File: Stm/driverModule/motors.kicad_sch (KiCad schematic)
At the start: 4 parts, among them U201 DRV8838, U202 DRV8838, U203 DRV8838, U204 VNH5019A-E

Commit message: Add Headers
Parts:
- added C201: 33nF, symbol Device:C
- added J201: Conn_02x05_Row_Letter_First, Connector_PinHeader_1.00mm:PinHeader_1x40_P1.00mm_Vertical, symbol Connector_Generic:Conn_02x05_Row_Letter_First
- added R201, R202, R205, R206: 1K, symbol Device:R_US
- added R203: 1K5, symbol Device:R_US
- added R204: 10K, symbol Device:R_US
- added R207, R208: 3K3, symbol Device:R_US
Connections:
- net +12V: now also U204.12 (VBAT)
- net +3V3: now also R201.1, R202.1, R207.1, R208.1
- net GND: now also C201.2, R203.2
- net MirrorMorotYA: now reaches U202.2 (OUT1)
- net MirrorMorotYA: now also J201.a2 (Pin_a2)
- net MirrorMotorYB: now reaches U202.3 (OUT2)
- net MirrorMotorYB: now also J201.a3 (Pin_a3)
- net MirrorMotorYEnable: now reaches U202.5 (EN)
- net MirrorYDirection: now reaches U202.6 (PH)
- net MirrorMotorXA: now reaches U203.2 (OUT1)
- net MirrorMotorXA: now also J201.b2 (Pin_b2)
- net MirrorMotorXB: now reaches U203.3 (OUT2)
- net MirrorMotorXB: now also J201.a4 (Pin_a4)
- net MirrorMotorXEnable: now reaches U203.5 (EN)
- net MirrorXDirection: now reaches U203.6 (PH)
- net at U204.10 (INB): now also R206.2, R208.2
- net at U204.4 (INA): now also R205.2, R207.2
- net at U204.5 (EN/DIAGA): now also R201.2
- net at U204.8 (CS): now also R203.1, R204.2
- net at U204.9 (EN/DIAGB): now also R202.2
- new net: C201.1, R204.1
- new net WindorMotorDirA: R205.1
- new net WindowMotorDirB: R206.1
- no-connect marks 0 -> 6
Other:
- moved on the sheet: U204

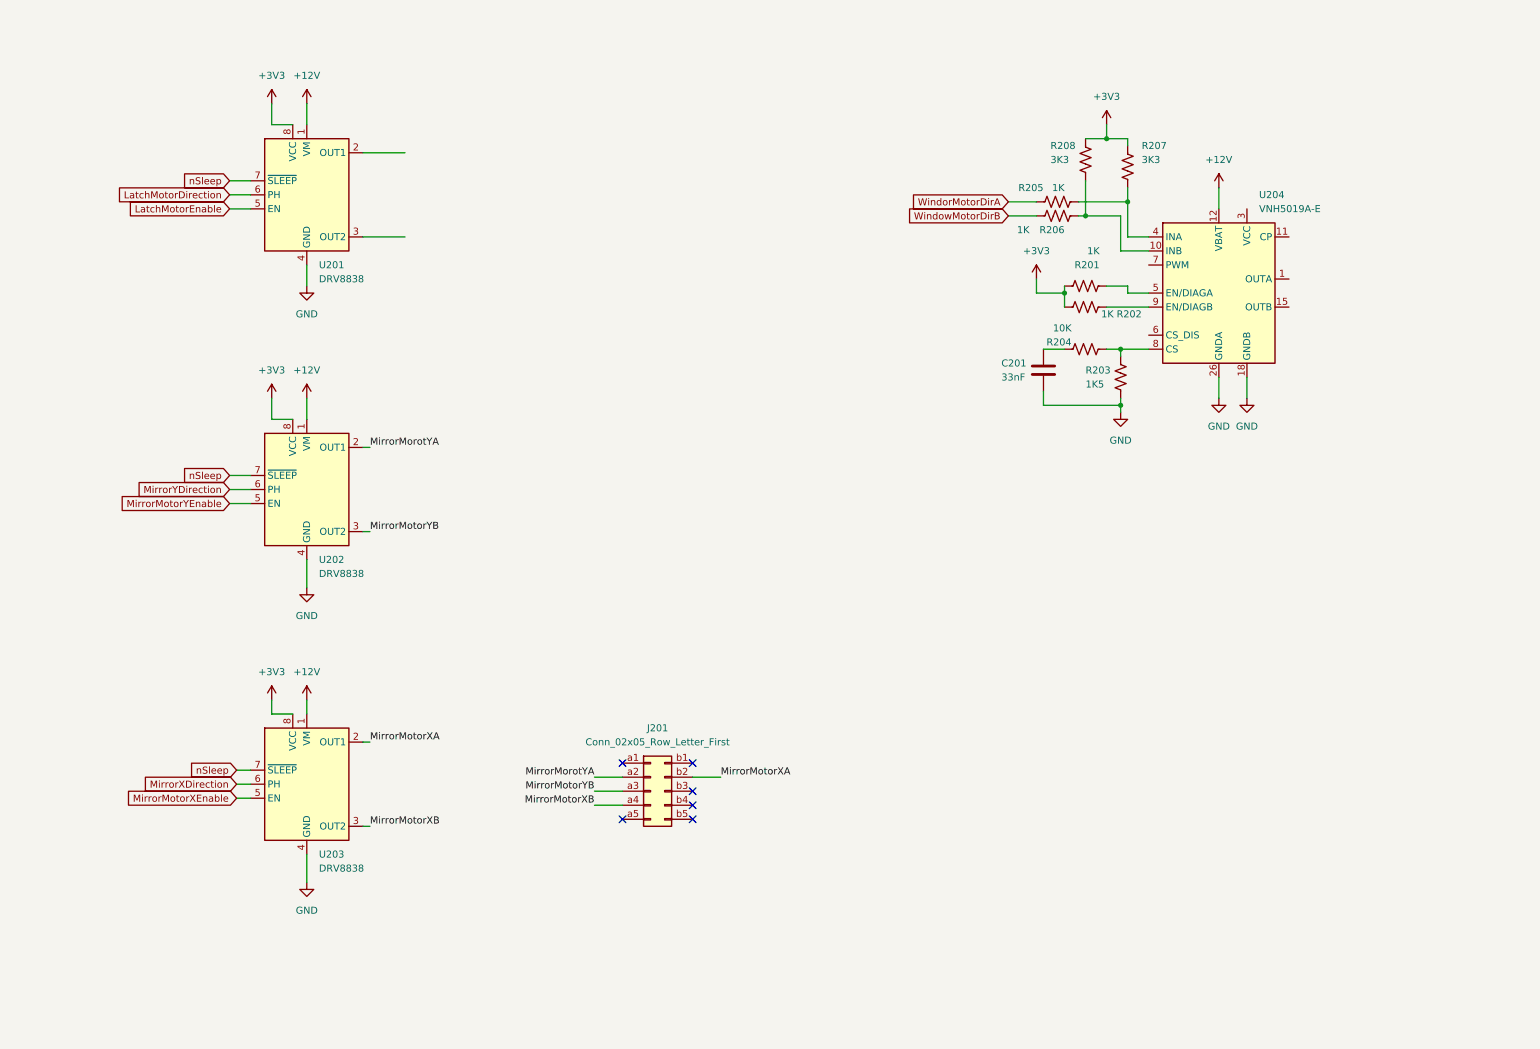
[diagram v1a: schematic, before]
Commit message: CD40109BNSR
Added low to high level shifter
and foot print
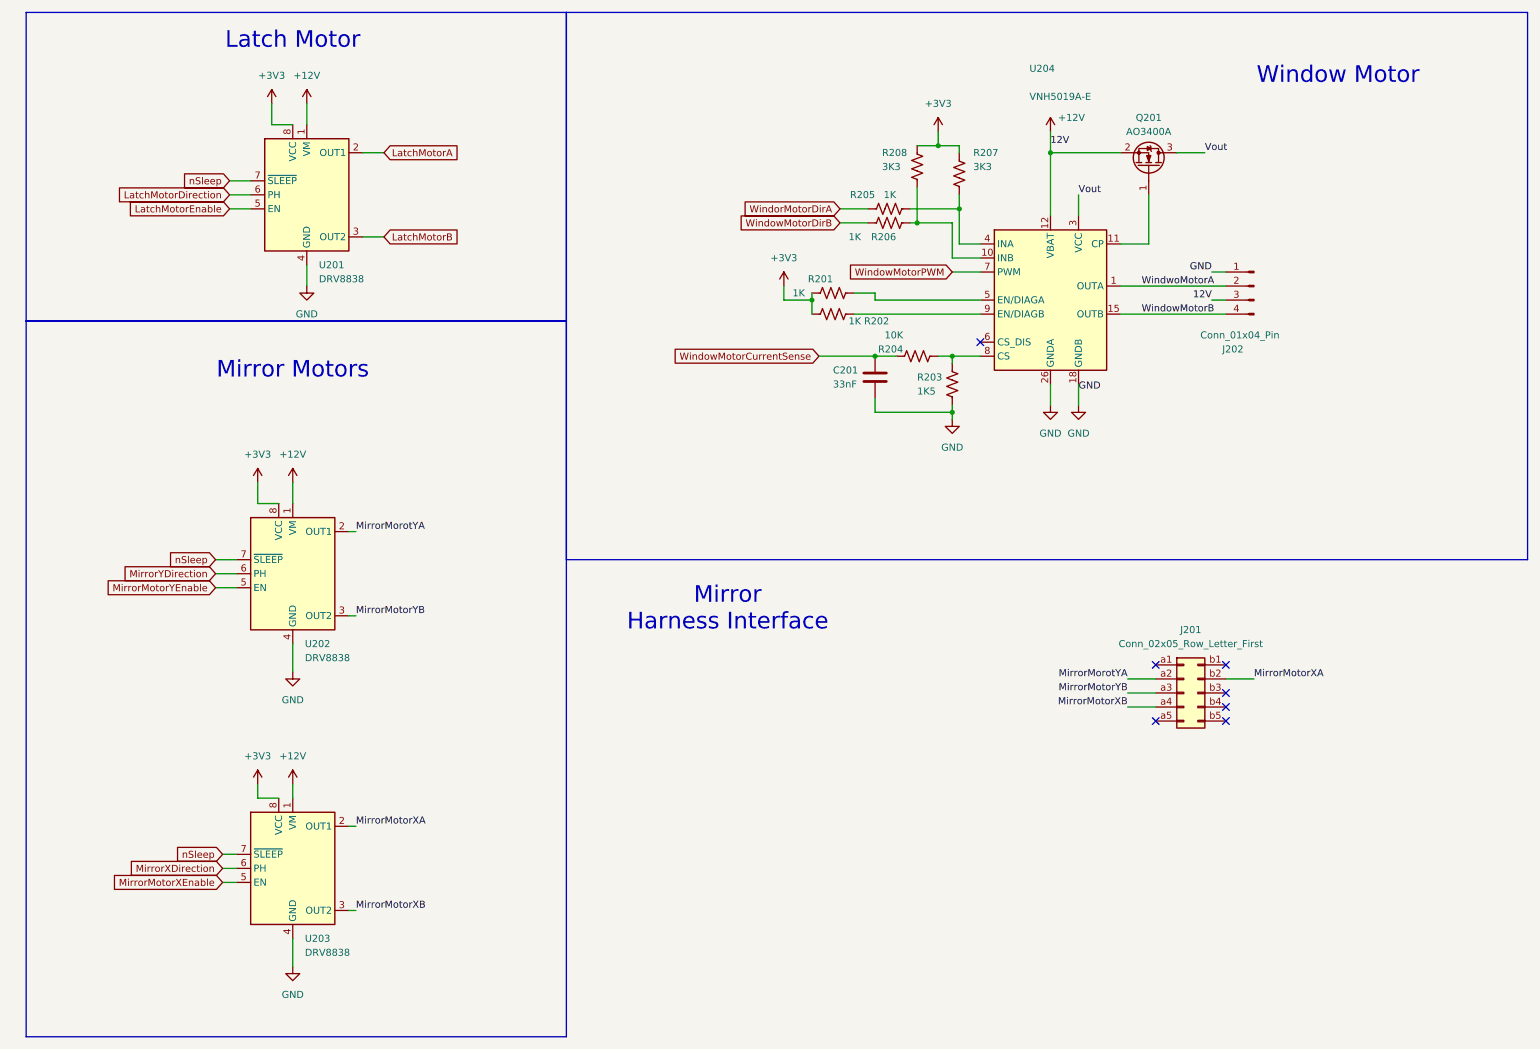
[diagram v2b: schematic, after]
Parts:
- added J202: Conn_01x04_Pin, Connector_Phoenix_MC_HighVoltage:PhoenixContact_MCV_1,5_4-G-5.08_1x04_P5.08mm_Vertical, symbol Connector:Conn_01x04_Pin
- added Q201: AO3400A, Package_TO_SOT_SMD:SOT-23, symbol Transistor_FET:AO3400A
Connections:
- net +12V: now also J202.3 (Pin_3), Q201.2 (S)
- net GND: now also J202.1 (Pin_1)
- net LatchMotorA: now reaches U201.2 (OUT1)
- net LatchMotorB: now reaches U201.3 (OUT2)
- net WindowMotorCurrentSense: now reaches C201.1, R204.1
- net WindwoMotorA: now reaches U204.1 (OUTA), U204.25 (OUTA), U204.30 (OUTA), U204.33 (OUTA)
- net WindwoMotorA: now also J202.2 (Pin_2)
- net at U204.11 (CP): now also Q201.1 (G)
- net Vout: now reaches U204.13 (VCC), U204.23 (VCC), U204.3 (VCC), U204.31 (VCC)
- net Vout: now also Q201.3 (D)
- net WindowMotorB: now reaches U204.15 (OUTB), U204.16 (OUTB), U204.21 (OUTB), U204.32 (OUTB)
- net WindowMotorB: now also J202.4 (Pin_4)
- net WindowMotorPWM: now reaches U204.7 (PWM)
- no-connect marks 6 -> 7
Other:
- note added: "Latch Motor"
- note added: "Mirror Harness Interface"
- note added: "Mirror Motors"
- note added: "Window Motor"
- moved on the sheet: C201, J201, R201, R202, R203, R204, R205, R206, R207, R208, U202, U203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

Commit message: Mirror Motors and key fob
Changed for a 3 half bridge semiconductor
Added level shift translator for key fob input
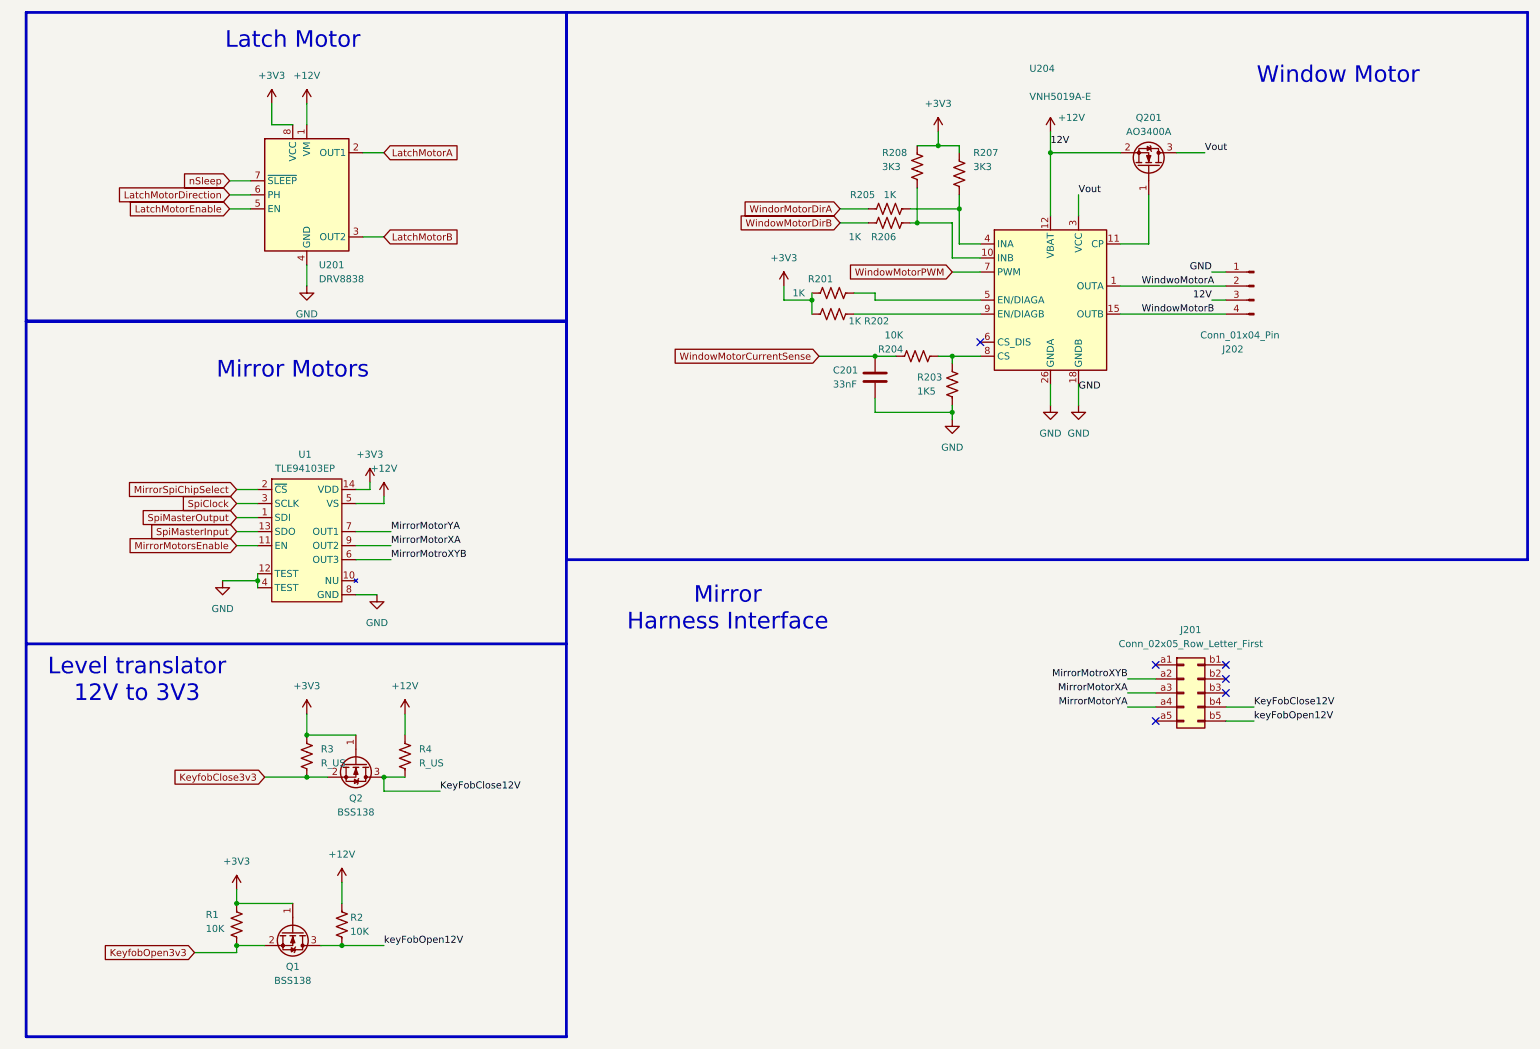
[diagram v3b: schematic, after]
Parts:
- removed U202, U203: DRV8838, Package_SON:WSON-8-1EP_2x2mm_P0.5mm_EP0.9x1.6mm, symbol Driver_Motor:DRV8838
- added Q1, Q2: BSS138, Package_TO_SOT_SMD:SOT-23, symbol Transistor_FET:BSS138
- added R1, R2: 10K, symbol Device:R_US
- added R3, R4: R_US, symbol Device:R_US
- added U1: TLE94103EP, Package_SO:Infineon_PG-TSDSO-14-22, symbol Local_symbols:TLE94103EP
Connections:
- net MirrorMotorYB is gone; now on net MirrorMotorXA: J201.a3 (Pin_a3)
- net +12V: now also R2.1, R4.1, U1.5 (VS)
- net +3V3: now also Q1.1 (G), Q2.1 (G), R1.1, R3.1, U1.14 (VDD)
- net GND: now also U1.12 (TEST), U1.4 (TEST), U1.8 (GND)
- net MirrorMotorXA: now also U1.9 (OUT2); no longer J201.b2 (Pin_b2)
- net KeyFobClose12V: now reaches J201.b4 (Pin_b4)
- net KeyFobClose12V: now also Q2.3 (D), R4.2
- net keyFobOpen12V: now reaches J201.b5 (Pin_b5)
- net keyFobOpen12V: now also Q1.3 (D), R2.2
- net MirrorMorotYA renamed MirrorMotroXYB
- net MirrorMotroXYB: now also U1.6 (OUT3)
- net MirrorMotorXB renamed MirrorMotorYA
- net MirrorMotorYA: now also U1.7 (OUT1)
- new net KeyfobClose3v3: Q2.2 (S), R3.2
- new net KeyfobOpen3v3: Q1.2 (S), R1.2
- new net MirrorMotorsEnable: U1.11 (EN)
- new net MirrorSpiChipSelect: U1.2 (~{CS})
- new net SpiClock: U1.3 (SCLK)
- new net SpiMasterInput: U1.13 (SDO)
- new net SpiMasterOutput: U1.1 (SDI)
- no-connect marks 7 -> 6
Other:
- note added: "Level translator 12V to 3V3"

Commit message: Connector
Removed processor and add a two SMD connectors to plug a MCU carrier board
Generate first Printed Circuit board layout
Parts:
- added C202: 47uF, Capacitor_SMD:CP_Elec_6.3x5.4_Nichicon, symbol Device:C_Polarized
- added C203: 0.1uF, symbol Device:C
- added C204, C205, C206, C207: 0u1F, symbol Device:C
- C201: footprint (none) -> Capacitor_SMD:C_0805_2012Metric
- J201: footprint Connector_PinHeader_1.00mm:PinHeader_1x40_P1.00mm_Vertical -> Connector_PinHeader_2.54mm:PinHeader_2x07_P2.54mm_Vertical
- R1, R2, R201, R202, R203, R204, R205, R206, R207, R208, R3, R4: footprint (none) -> Resistor_SMD:R_0402_1005Metric_Pad0.72x0.64mm_HandSolder
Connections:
- net +12V: now also C204.1, C206.1
- net +3V3: now also C205.1, C207.1
- net GND: now also C202.2, C203.2, C204.2, C205.2, C206.2, C207.2
- net Vout: now also C202.1, C203.1
- net WindorMotorDirA renamed WindowMotorDirA

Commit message: Symbols
Changed some symbols
Components placements
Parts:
- removed J201: Conn_02x05_Row_Letter_First, Connector_PinHeader_2.54mm:PinHeader_2x07_P2.54mm_Vertical, symbol Connector_Generic:Conn_02x05_Row_Letter_First
- removed Q201: AO3400A, Package_TO_SOT_SMD:SOT-23, symbol Transistor_FET:AO3400A
- added J1: Conn_02x05_Odd_Even, Connector_PinHeader_2.54mm:PinHeader_2x05_P2.54mm_Vertical, symbol Connector_Generic:Conn_02x05_Odd_Even
- added Q3: AON7410, Local_Footprints:DFN_3X3_EP, symbol Local_symbols:AON7410
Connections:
- net +12V: now also Q3.1 (S_1), Q3.2 (S_2), Q3.3 (S_3)
- net KeyFobClose12V: now also J1.8 (Pin_8)
- net MirrorMotorXA: now also J1.5 (Pin_5)
- net MirrorMotorYA: now also J1.7 (Pin_7)
- net Vout: now also Q3.5 (D_1), Q3.6 (D_2), Q3.7 (D_3), Q3.8 (D_4)
- net keyFobOpen12V: now also J1.10 (Pin_10)
- net INA: now reaches R205.2, R207.2, U204.4 (INA)
- net INB: now reaches R206.2, R208.2, U204.10 (INB)
- net CS: now reaches R203.1, R204.2, U204.8 (CS)
- net EN/DIAGA: now reaches R201.2, U204.5 (EN/DIAGA)
- net G: now reaches U204.11 (CP)
- net G: now also Q3.4 (G)
- net EN/DIAGB: now reaches R202.2, U204.9 (EN/DIAGB)
- net MirrorMotroXYB renamed MirrorMotorXYB
- net MirrorMotorXYB: now also J1.3 (Pin_3)
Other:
- moved on the sheet: C202, C203
